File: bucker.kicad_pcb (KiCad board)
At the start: 2 copper layers, 70 x 35 mm, 29 parts, among them SW1 SW_SPDT, SW2 SW_DIP_x4, U1 TPS54231

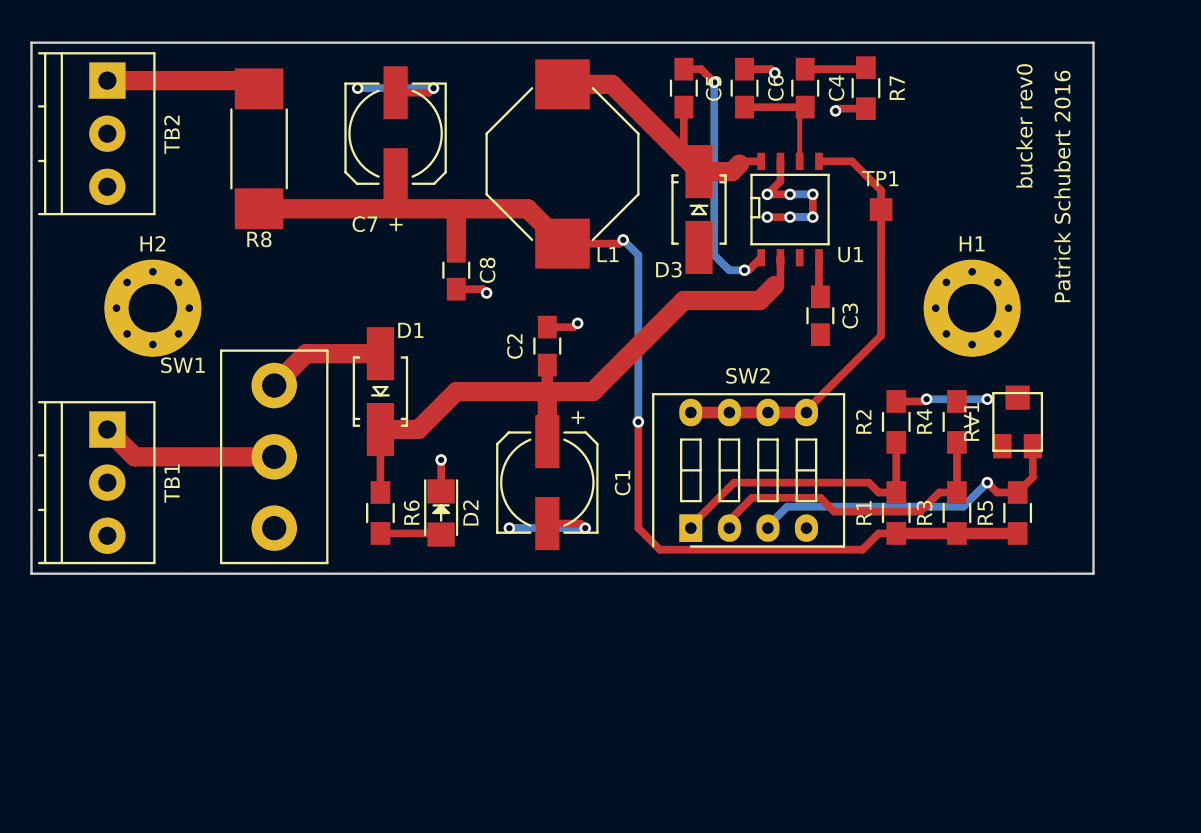
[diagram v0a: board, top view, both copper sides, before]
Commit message: Added current sense amp and connector.
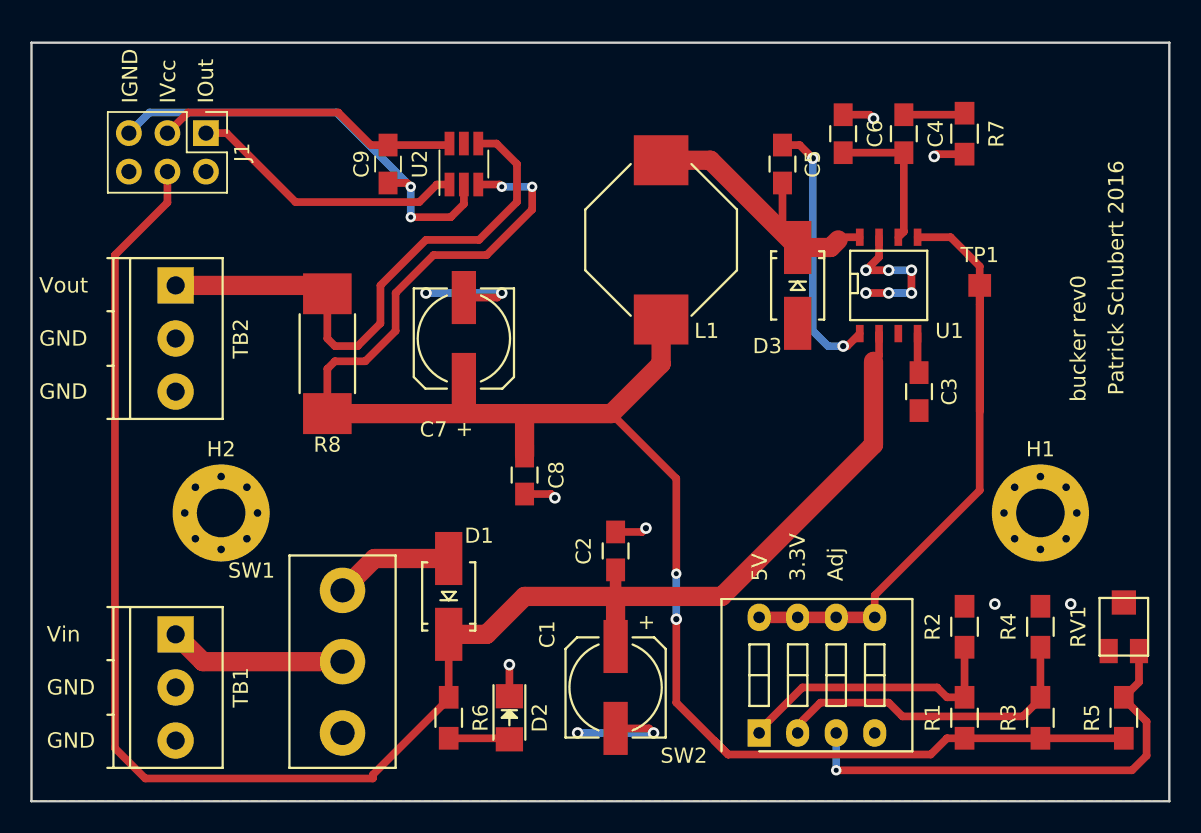
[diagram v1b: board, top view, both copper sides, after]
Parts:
- added C9: 0.1uF, Capacitors_SMD:C_0805_HandSoldering, F.Cu at (23.5, 8.00)
- added J1: CONN_02X03, Pin_Headers:Pin_Header_Straight_2x03_Pitch2.54mm, F.Cu at (11.5, 5.96)
- added U2: LMP8640, TO_SOT_Packages_SMD:SOT-23-6_Handsoldering, F.Cu at (28.5, 8.00)
- R6: value 2k -> 2.2k
- RV1: value POT -> 10k
- moved R5 15.2 mm to (72.0, 44.5)
- moved RV1 15.2 mm to (72.0, 38.5)
- moved R3 14.6 mm to (66.5, 44.5)
- moved R4 14.6 mm to (66.5, 38.5)
- moved C1 14.2 mm to (38.5, 42.5)
- moved C2 14.2 mm to (38.5, 33.5)
- moved C7 14.2 mm to (28.5, 19.5)
- moved C8 14.2 mm to (32.5, 28.5)
- moved D1 14.2 mm to (27.5, 36.5)
- moved D2 14.2 mm to (31.5, 44.5)
- moved H1 14.2 mm to (66.5, 31.0)
- moved H2 14.2 mm to (12.5, 31.0)
- moved R1 14.2 mm to (61.5, 44.5)
- moved R2 14.2 mm to (61.5, 38.5)
- moved R6 14.2 mm to (27.5, 44.5)
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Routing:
- net VCC: track 41.4 -> 114.9 mm
- net /INSTR_GND: track 0.00 -> 29.9 mm, vias 0 -> 2
- net /VOUT: track 83.6 -> 112.2 mm, vias 2 -> 4
- net Net-(R8-Pad1): track 10.2 -> 36.9 mm
- net /SENSE_IN: track 36.7 -> 61.9 mm
- net /INSTR_VCC: track 0.00 -> 20.1 mm
- net Net-(J1-Pad1): track 0.00 -> 18.4 mm
- net Net-(R5-Pad2): track 21.5 -> 31.4 mm
- net GND: track 41.8 -> 35.7 mm
- net Net-(C4-Pad2): track 7.73 -> 10.2 mm
- net Net-(R3-Pad2): track 20.5 -> 21.5 mm
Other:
- board size 70 x 35 mm -> 75 x 50 mm
- board text added: "3.3V"
- board text added: "5V"
- board text added: "Adj"
- board text added: "GND"
- board text added: "IGND"
- board text added: "IOut"
- board text added: "IVcc"
- board text added: "Vin"
- board text added: "Vout"

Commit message: Aligned mounting holes and terminal blocks.
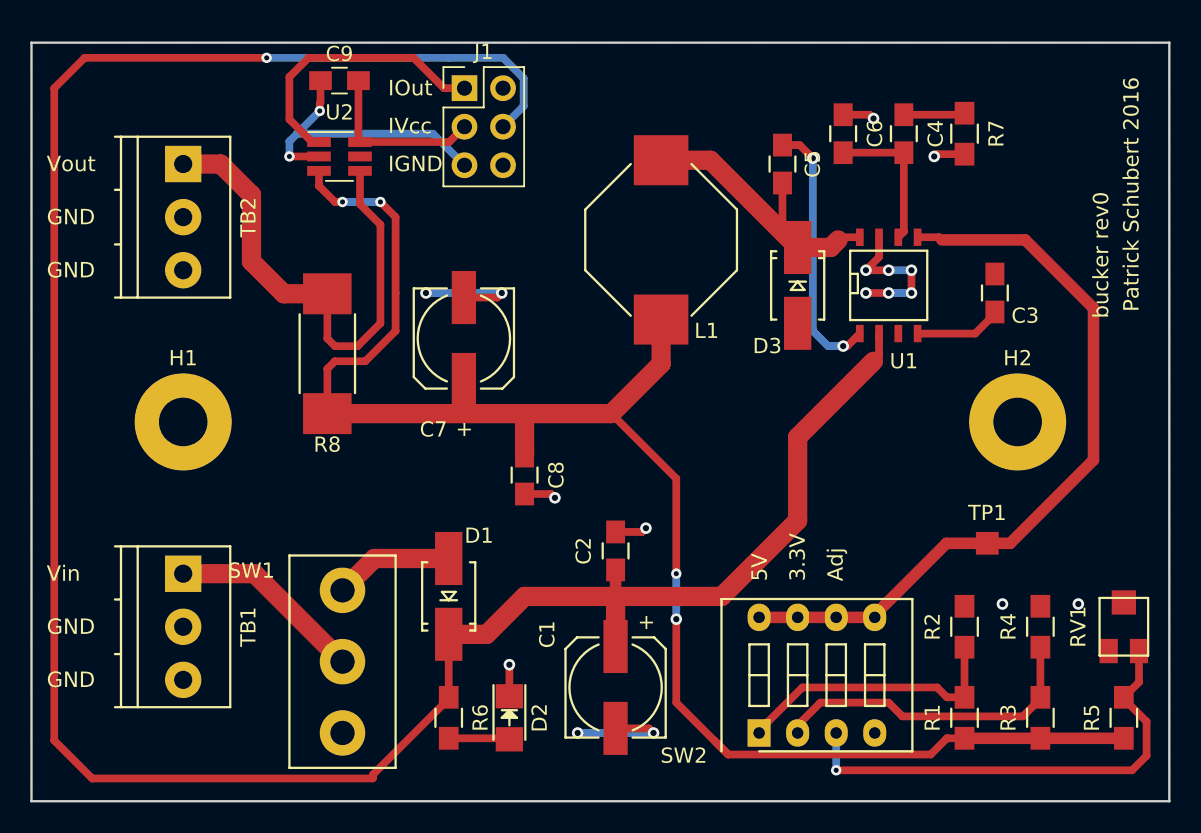
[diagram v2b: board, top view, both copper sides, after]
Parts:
- H1, H2: value M3 screw -> PLATED_HOLE; footprint Mounting_Holes:MountingHole_3.2mm_M3_Pad_Via -> Mounting_Holes:MountingHole_3.2mm_M3_Pad
- moved H1 56.8 mm to (10.0, 25.0)
- moved H2 52.8 mm to (65.0, 25.0)
- moved J1 17.3 mm to (28.5, 3.00), turned to 0 degrees
- moved TP1 17.0 mm to (63.0, 33.0)
- moved U2 8.22 mm to (20.3, 7.50), turned to 0 degrees
- moved C3 8.20 mm to (63.5, 16.5), turned to 270 degrees
- moved TB2 8.02 mm to (10.0, 8.00)
- moved C9 6.36 mm to (20.3, 2.50), turned to 0 degrees
- moved TB1 4.03 mm to (10.0, 35.0)
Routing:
- net VCC: track 114.9 -> 158.7 mm, vias 0 -> 1
- net /INSTR_GND: track 29.9 -> 19.7 mm
- net /INSTR_VCC: track 20.1 -> 11.4 mm
- net /VOUT: track 112.2 -> 107.7 mm
- net Net-(C3-Pad2): track 2.61 -> 5.76 mm
- net /SENSE_IN: track 61.9 -> 65.1 mm
- net Net-(R8-Pad1): track 36.9 -> 34.3 mm
- net Net-(SW1-Pad2): track 11.7 -> 12.9 mm
- net GND: vias 17 -> 15
- net (no net): vias 0 -> 2
